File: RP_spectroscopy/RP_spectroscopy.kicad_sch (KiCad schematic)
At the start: 0 parts

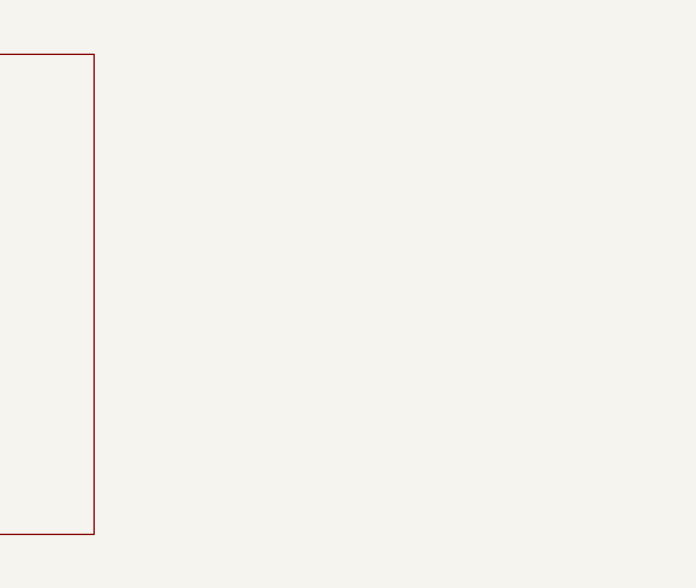
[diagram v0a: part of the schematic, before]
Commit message: Continued with the connection scheet
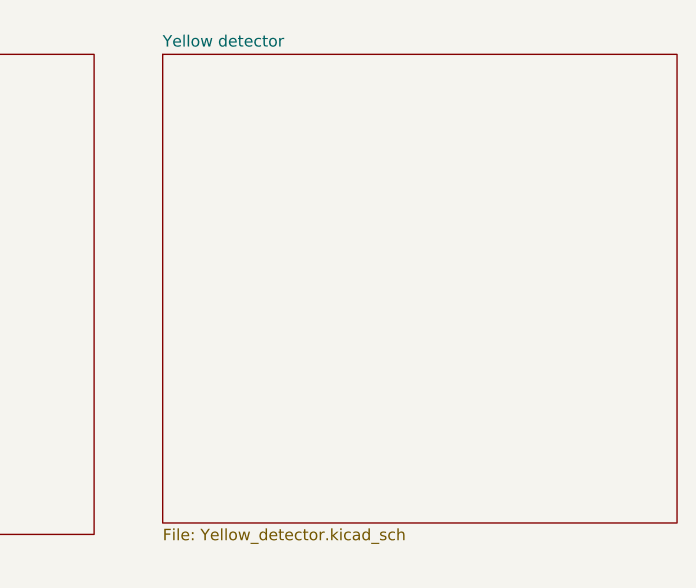
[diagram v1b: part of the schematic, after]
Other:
- added sheet Yellow detector (Yellow_detector.kicad_sch)
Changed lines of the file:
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@@
+	)
+	(sheet
+		(at 220.98 21.59)
+		(size 57.15 52.07)
+		(exclude_from_sim no)
+		(in_bom yes)
+		(on_board yes)
+		(dnp no)
+		(fields_autoplaced yes)
+		(stroke
+			(width 0.1524)
+			(type solid)
+		)
+		(fill
+			(color 0 0 0 0.0000)
+		)
+		(property "Sheetname" "Yellow detector"
+			(at 220.98 20.8784 0)
+			(effects
+				(font
+					(size 1.27 1.27)
+				)
+				(justify left bottom)
+			)
+		)
+		(property "Sheetfile" "Yellow_detector.kicad_sch"
+			(at 220.98 74.2446 0)
+			(effects
+				(font
+					(size 1.27 1.27)
+				)
+				(justify left top)
+			)
+		)
+		(instances
+			(project "RP_spectroscopy"
+				(path "/dd9ac3ef-6a3a-4df6-b083-1a4e73093ea8"
+					(page "5")
+				)
+			)
+		)
 	)
 	(sheet

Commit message: Check of the availability of all the components and of the footprints. Added the demultiplexer part of the circuit. Some graphical changes. Changed the values of some R in order to match the ones available in the officina elettronica.
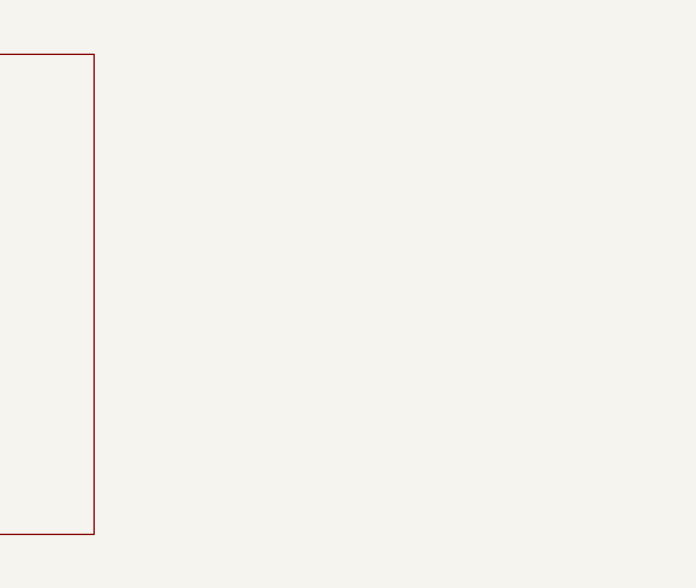
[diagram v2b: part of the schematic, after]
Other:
- removed sheet Yellow detector
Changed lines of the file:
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@@
-	)
-	(sheet
-		(at 220.98 21.59)
-		(size 57.15 52.07)
-		(exclude_from_sim no)
-		(in_bom yes)
-		(on_board yes)
-		(dnp no)
-		(fields_autoplaced yes)
-		(stroke
-			(width 0.1524)
-			(type solid)
-		)
-		(fill
-			(color 0 0 0 0.0000)
-		)
-		(property "Sheetname" "Yellow detector"
-			(at 220.98 20.8784 0)
-			(effects
-				(font
-					(size 1.27 1.27)
-				)
-				(justify left bottom)
-			)
-		)
-		(property "Sheetfile" "Yellow_detector.kicad_sch"
-			(at 220.98 74.2446 0)
-			(effects
-				(font
-					(size 1.27 1.27)
-				)
-				(justify left top)
-			)
-		)
-		(instances
-			(project "RP_spectroscopy"
-				(path "/dd9ac3ef-6a3a-4df6-b083-1a4e73093ea8"
-					(page "5")
-				)
-			)
-		)
 	)
 	(sheet
